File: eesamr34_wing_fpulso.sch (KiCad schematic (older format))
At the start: 19 parts, among them J3 Conn_01x02_Male, P1 SolderJumper_3_Bridged12, Q1 BS250, U2 4069

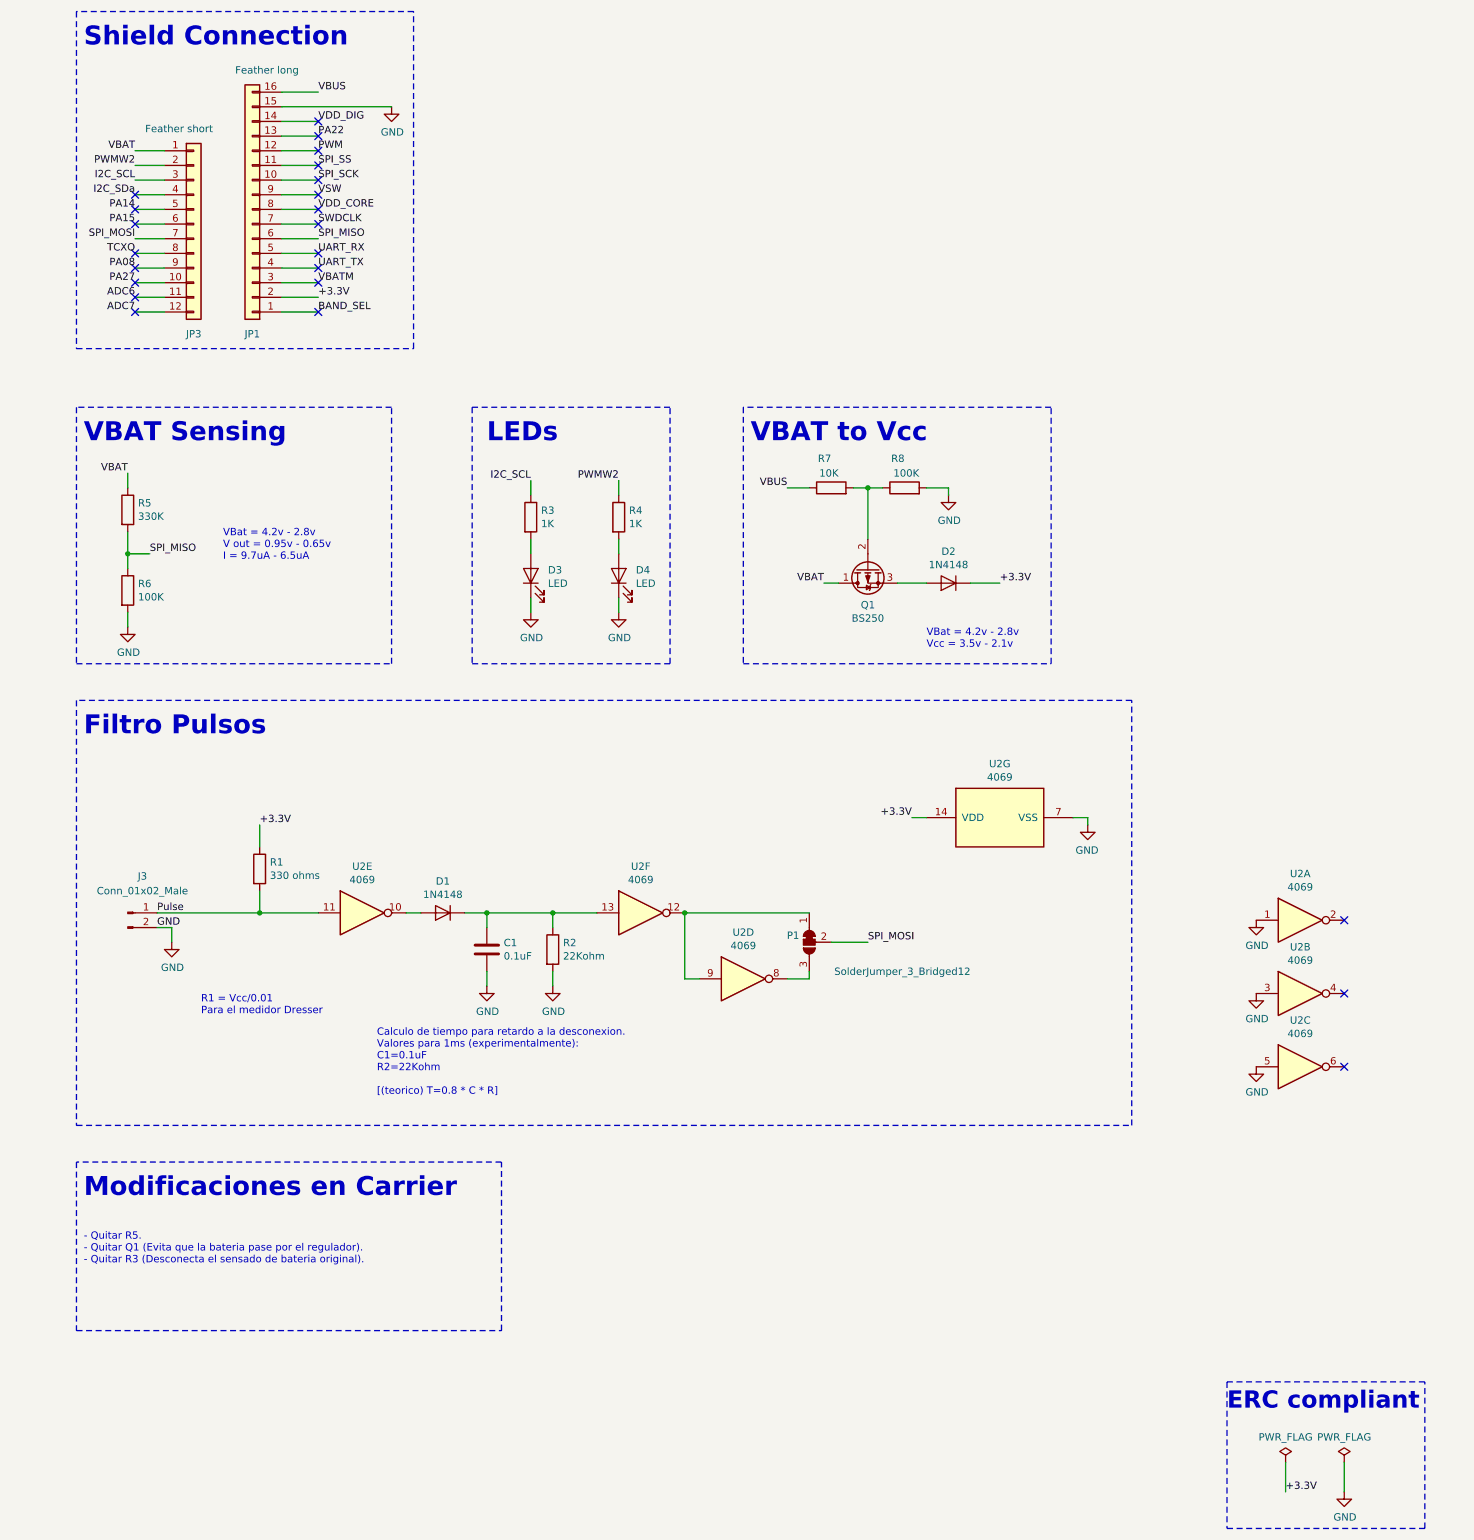
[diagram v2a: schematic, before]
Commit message: Reducido consumo de pullup y filtro
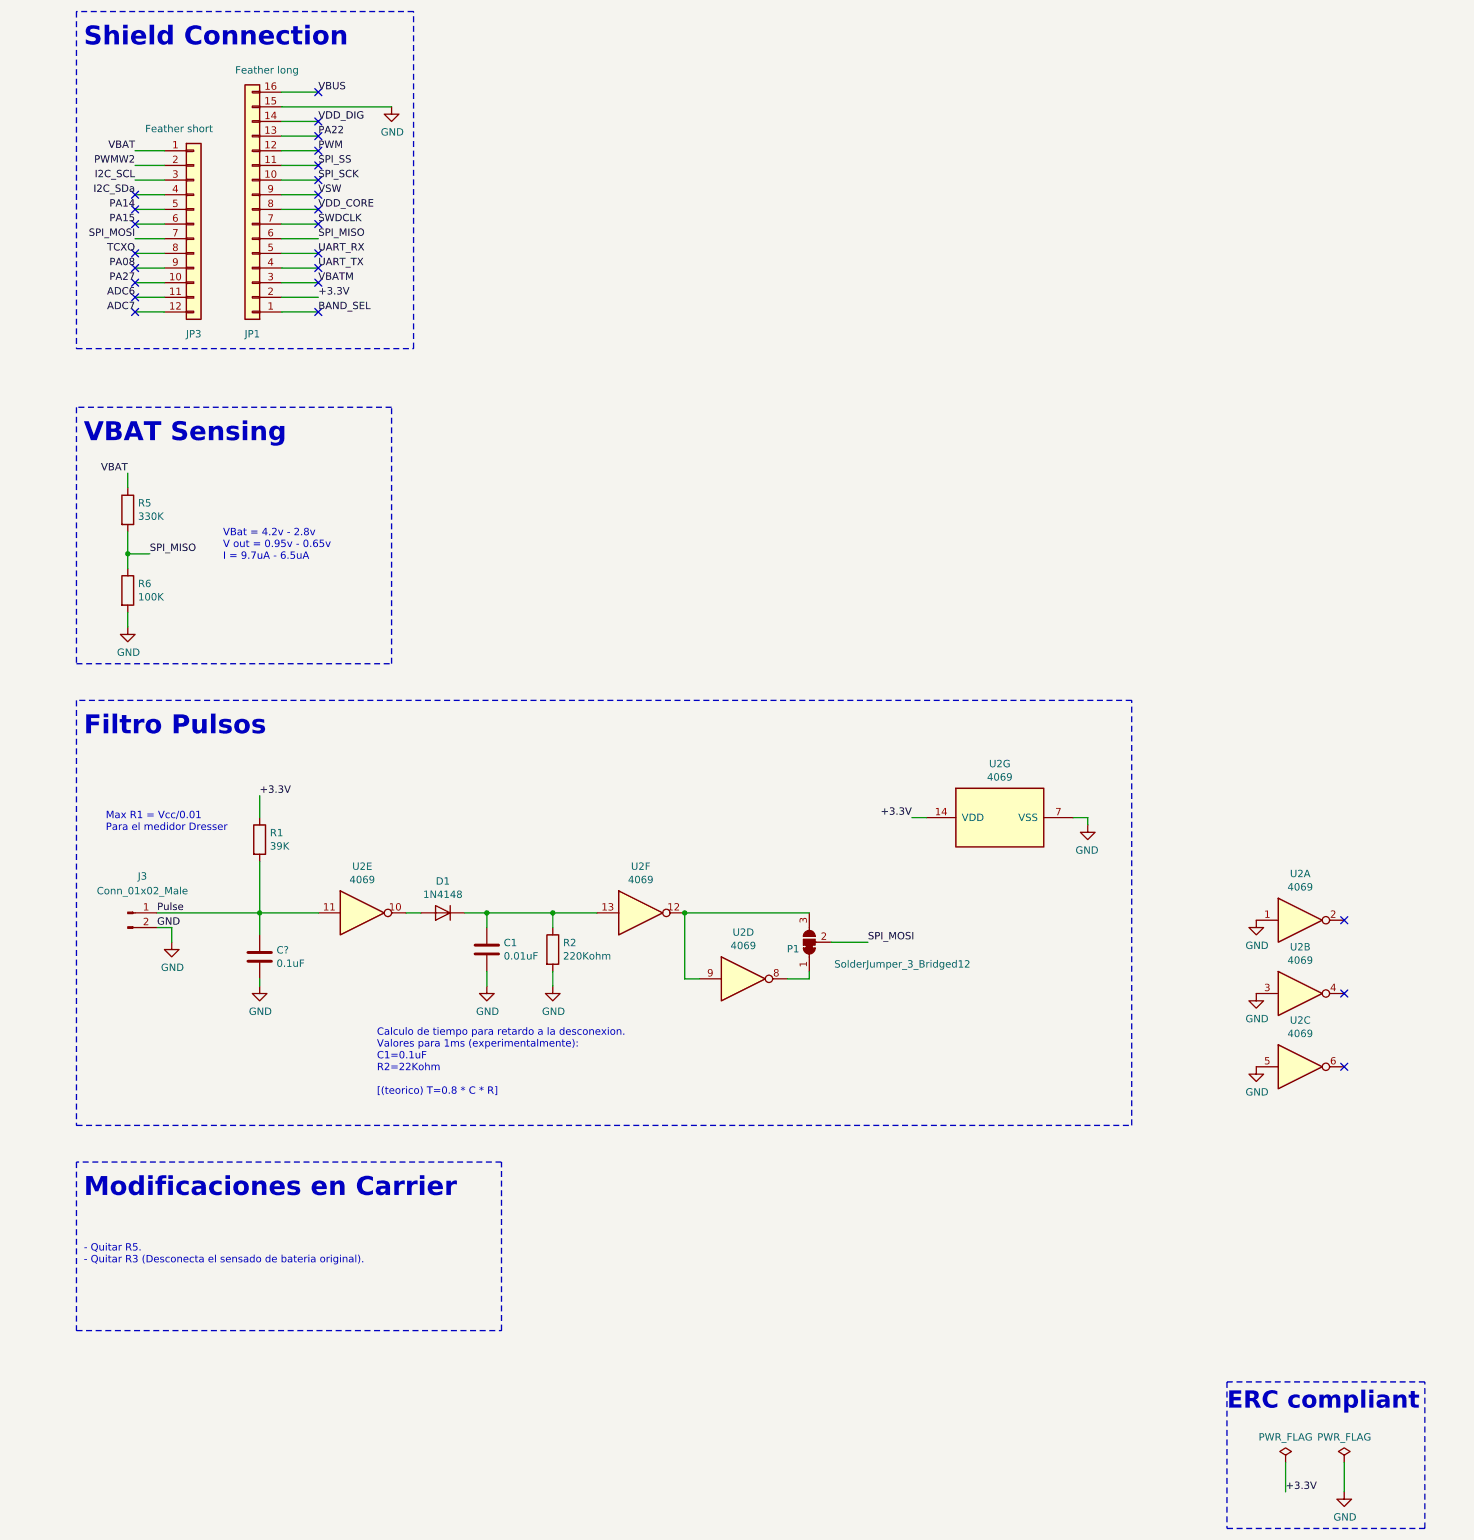
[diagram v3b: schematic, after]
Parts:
- removed D2: 1N4148, Diode_THT:D_DO-35_SOD27_P7.62mm_Horizontal, symbol Diode:1N4148
- removed D3, D4: LED, LED_THT:LED_D5.0mm, symbol Device:LED
- removed Q1: BS250, Package_TO_SOT_THT:TO-92_Inline, symbol Transistor_FET:BS250
- removed R3, R4: 1K, Resistor_THT:R_Axial_DIN0207_L6.3mm_D2.5mm_P10.16mm_Horizontal, symbol Device:R
- removed R7: 10K, Resistor_THT:R_Axial_DIN0207_L6.3mm_D2.5mm_P10.16mm_Horizontal, symbol Device:R
- removed R8: 100K, Resistor_THT:R_Axial_DIN0207_L6.3mm_D2.5mm_P10.16mm_Horizontal, symbol Device:R
- added C?: 0.1uF, Capacitor_THT:C_Disc_D5.0mm_W2.5mm_P2.50mm, symbol Device:C
- C1: value 0.1uF -> 0.01uF
- R1: value 330 ohms -> 39K
- R2: value 22Kohm -> 220Kohm
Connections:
- net GND: now also C?.2
- net Pulse: now also C?.1
- net at U2.12, U2.9: now also P1.3 (B); no longer P1.1 (A)
- net at U2.8: now also P1.1 (A); no longer P1.3 (B)
- no-connect marks 23 -> 24
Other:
- note added: "- Quitar R5.\n- Quitar R3 (Desconecta el sensado de bateria original)."
- note added: "Max R1 = Vcc/0.01\nPara el medidor Dresser"
- note removed: "- Quitar R5.\n- Quitar Q1 (Evita que la bateria pase por el regulador).\n- Quitar R3 (Desconecta el sensado de bateria original)."
- note removed: "LEDs"
- note removed: "R1 = Vcc/0.01\nPara el medidor Dresser"
- note removed: "VBAT to Vcc"
- note removed: "VBat = 4.2v - 2.8v\nVcc = 3.5v - 2.1v"
- moved on the sheet: R1
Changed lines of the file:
@@
 P 3800 7100
 F 0 "R2" H 3870 7146 50  0000 L CNN
-F 1 "22Kohm" H 3870 7055 50  0000 L CNN
+F 1 "220Kohm" H 3870 7055 50  0000 L CNN
 F 2 "Resistor_THT:R_Axial_DIN0207_L6.3mm_D2.5mm_P10.16mm_Horizontal" V 3730 7100 50  0001 C CNN
 F 3 "~" H 3800 7100 50  0001 C CNN
@@
 P 3350 7100
 F 0 "C1" H 3465 7146 50  0000 L CNN
-F 1 "0.1uF" H 3465 7055 50  0000 L CNN
+F 1 "0.01uF" H 3465 7055 50  0000 L CNN
 F 2 "Capacitor_THT:C_Disc_D5.0mm_W2.5mm_P2.50mm" H 3388 6950 50  0001 C CNN
 F 3 "~" H 3350 7100 50  0001 C CNN
@@
 L Device:R R1
 U 1 1 5F5899B8
-P 1800 6550
-F 0 "R1" H 1870 6596 50  0000 L CNN
-F 1 "330 ohms" H 1870 6505 50  0000 L CNN
-F 2 "Resistor_THT:R_Axial_DIN0207_L6.3mm_D2.5mm_P10.16mm_Horizontal" V 1730 6550 50  0001 C CNN
-F 3 "~" H 1800 6550 50  0001 C CNN
-	1    1800 6550
-	1    0    0    -1
-$EndComp
-Wire Wire Line
-	1800 6850 1800 6700
-Wire Wire Line
-	1800 6250 1800 6400
+P 1800 6350
+F 0 "R1" H 1870 6396 50  0000 L CNN
+F 1 "39K" H 1870 6305 50  0000 L CNN
+F 2 "Resistor_THT:R_Axial_DIN0207_L6.3mm_D2.5mm_P10.16mm_Horizontal" V 1730 6350 50  0001 C CNN
+F 3 "~" H 1800 6350 50  0001 C CNN
+	1    1800 6350
+	1    0    0    -1
+$EndComp
+Wire Wire Line
+	1800 6050 1800 6200
 Wire Wire Line
 	3350 6950 3350 6850
@@
 P 5550 7050
 F 0 "P1" V 5504 7118 50  0000 L CNN
-F 1 "SolderJumper_3_Bridged12" V 5750 5950 50  0000 L CNN
+F 1 "SolderJumper_3_Bridged12" V 5400 5950 50  0000 L CNN
 F 2 "Jumper:SolderJumper-3_P1.3mm_Bridged12_Pad1.0x1.5mm" H 5550 7050 50  0001 C CNN
 F 3 "~" H 5550 7050 50  0001 C CNN
 	1    5550 7050
-	0    -1   1    0
+	0    -1   -1   0
 $EndComp
 Wire Wire Line
@@
 Text Notes 2600 8100 0    50   ~ 0
 Calculo de tiempo para retardo a la desconexion.\nValores para 1ms (experimentalmente):\nC1=0.1uF\nR2=22Kohm\n\n[(teorico) T=0.8 * C * R]
-Text Notes 1400 7550 0    50   ~ 0
-R1 = Vcc/0.01\nPara el medidor Dresser
-Text Label 1800 6250 0    50   ~ 0
+Text Notes 750  6300 0    50   ~ 0
+Max R1 = Vcc/0.01\nPara el medidor Dresser
+Text Label 1800 6050 0    50   ~ 0
 +3.3V
 Text Notes 600  5650 0    129  ~ 26
@@
 ADC6
 Text Notes 600  9250 0    50   ~ 0
-- Quitar R5.\n- Quitar Q1 (Evita que la bateria pase por el regulador).\n- Quitar R3 (Desconecta el sensado de bateria original).
+- Quitar R5.\n- Quitar R3 (Desconecta el sensado de bateria original).
 Text Notes 600  8800 0    129  ~ 26
 Modificaciones en Carrier\n
@@
 Text Notes 1550 4450 0    50   ~ 0
 VBat = 4.2v - 2.8v\nV out = 0.95v - 0.65v\nI = 9.7uA - 6.5uA
-Text Notes 6350 5050 0    50   ~ 0
-VBat = 4.2v - 2.8v\nVcc = 3.5v - 2.1v
 Wire Wire Line
 	900  4400 900  4500
@@
 	1    0    0    -1
 $EndComp
-Text Notes 3350 3650 0    129  ~ 26
-LEDs
-Wire Wire Line
-	4250 3900 4250 4000
-Wire Wire Line
-	3650 3900 3650 4000
-Text Label 3650 3900 2    50   ~ 0
-I2C_SCL
-Text Label 4250 3900 2    50   ~ 0
-PWMW2
-Wire Wire Line
-	4250 4700 4250 4800
-Wire Wire Line
-	3650 4700 3650 4800
-Wire Wire Line
-	4250 4300 4250 4400
-Wire Wire Line
-	3650 4300 3650 4400
-$Comp
-L power:GND #PWR01
-U 1 1 5F964773
-P 4250 4800
-F 0 "#PWR01" H 4250 4550 50  0001 C CNN
-F 1 "GND" H 4255 4627 50  0000 C CNN
-F 2 "" H 4250 4800 50  0001 C CNN
-F 3 "" H 4250 4800 50  0001 C CNN
-	1    4250 4800
-	1    0    0    -1
-$EndComp
-$Comp
-L Device:LED D4
-U 1 1 5F96476D
-P 4250 4550
-F 0 "D4" V 4289 4433 50  0000 R CNN
-F 1 "LED" V 4198 4433 50  0000 R CNN
-F 2 "LED_THT:LED_D5.0mm" H 4250 4550 50  0001 C CNN
-F 3 "~" H 4250 4550 50  0001 C CNN
-	1    4250 4550
-	0    -1   -1   0
-$EndComp
-$Comp
-L Device:R R4
-U 1 1 5F964767
-P 4250 4150
-F 0 "R4" H 4320 4196 50  0000 L CNN
-F 1 "1K" H 4320 4105 50  0000 L CNN
-F 2 "Resistor_THT:R_Axial_DIN0207_L6.3mm_D2.5mm_P10.16mm_Horizontal" V 4180 4150 50  0001 C CNN
-F 3 "~" H 4250 4150 50  0001 C CNN
-	1    4250 4150
-	1    0    0    -1
-$EndComp
-Text Notes 5150 3650 0    129  ~ 26
-VBAT to Vcc
-Wire Wire Line
-	6650 4600 6850 4600
-Wire Wire Line
-	6150 4600 6350 4600
-Text Label 6850 4600 0    50   ~ 0
-+3.3V
-Text Label 5650 4600 2    50   ~ 0
-VBAT
-$Comp
-L Diode:1N4148 D2
-U 1 1 5F937EA6
-P 6500 4600
-F 0 "D2" H 6500 4384 50  0000 C CNN
-F 1 "1N4148" H 6500 4475 50  0000 C CNN
-F 2 "Diode_THT:D_DO-35_SOD27_P7.62mm_Horizontal" H 6500 4425 50  0001 C CNN
-F 3 "https://assets.nexperia.com/documents/data-sheet/1N4148_1N4448.pdf" H 6500 4600 50  0001 C CNN
-	1    6500 4600
-	-1   0    0    1
-$EndComp
-$Comp
-L power:GND #PWR0106
-U 1 1 5F5899F4
-P 3650 4800
-F 0 "#PWR0106" H 3650 4550 50  0001 C CNN
-F 1 "GND" H 3655 4627 50  0000 C CNN
-F 2 "" H 3650 4800 50  0001 C CNN
-F 3 "" H 3650 4800 50  0001 C CNN
-	1    3650 4800
-	1    0    0    -1
-$EndComp
-$Comp
-L Device:LED D3
-U 1 1 5F5899EE
-P 3650 4550
-F 0 "D3" V 3689 4433 50  0000 R CNN
-F 1 "LED" V 3598 4433 50  0000 R CNN
-F 2 "LED_THT:LED_D5.0mm" H 3650 4550 50  0001 C CNN
-F 3 "~" H 3650 4550 50  0001 C CNN
-	1    3650 4550
-	0    -1   -1   0
-$EndComp
-$Comp
-L Device:R R3
-U 1 1 5F5899E8
-P 3650 4150
-F 0 "R3" H 3720 4196 50  0000 L CNN
-F 1 "1K" H 3720 4105 50  0000 L CNN
-F 2 "Resistor_THT:R_Axial_DIN0207_L6.3mm_D2.5mm_P10.16mm_Horizontal" V 3580 4150 50  0001 C CNN
-F 3 "~" H 3650 4150 50  0001 C CNN
-	1    3650 4150
-	1    0    0    -1
-$EndComp
-$Comp
-L Transistor_FET:BS250 Q1
-U 1 1 5FAA13A5
-P 5950 4500
-F 0 "Q1" V 6199 4500 50  0000 C CNN
-F 1 "BS250" V 6290 4500 50  0000 C CNN
-F 2 "Package_TO_SOT_THT:TO-92_Inline" H 6150 4425 50  0001 L CIN
-F 3 "http://www.vishay.com/docs/70209/70209.pdf" H 5950 4500 50  0001 L CNN
-	1    5950 4500
-	0    -1   1    0
-$EndComp
-Wire Wire Line
-	5650 4600 5750 4600
-$Comp
-L Device:R R8
-U 1 1 5FAA87B2
-P 6200 3950
-F 0 "R8" V 6400 3950 50  0000 L CNN
-F 1 "100K" V 6300 3850 50  0000 L CNN
-F 2 "Resistor_THT:R_Axial_DIN0207_L6.3mm_D2.5mm_P10.16mm_Horizontal" V 6130 3950 50  0001 C CNN
-F 3 "~" H 6200 3950 50  0001 C CNN
-	1    6200 3950
-	0    -1   -1   0
-$EndComp
-$Comp
-L power:GND #PWR05
-U 1 1 5FAA8E51
-P 6500 4000
-F 0 "#PWR05" H 6500 3750 50  0001 C CNN
-F 1 "GND" H 6505 3827 50  0000 C CNN
-F 2 "" H 6500 4000 50  0001 C CNN
-F 3 "" H 6500 4000 50  0001 C CNN
-	1    6500 4000
-	1    0    0    -1
-$EndComp
-Text Label 5400 3950 2    50   ~ 0
-VBUS
-Wire Wire Line
-	5400 3950 5550 3950
-Wire Wire Line
-	5950 4300 5950 3950
-Wire Wire Line
-	5950 3950 5850 3950
-$Comp
-L Device:R R7
-U 1 1 5FAA7900
-P 5700 3950
-F 0 "R7" V 5900 3950 50  0000 L CNN
-F 1 "10K" V 5800 3900 50  0000 L CNN
-F 2 "Resistor_THT:R_Axial_DIN0207_L6.3mm_D2.5mm_P10.16mm_Horizontal" V 5630 3950 50  0001 C CNN
-F 3 "~" H 5700 3950 50  0001 C CNN
-	1    5700 3950
-	0    -1   -1   0
-$EndComp
-Wire Notes Line
-	5100 3400 5100 5150
-Wire Notes Line
-	5100 5150 7200 5150
-Wire Notes Line
-	7200 5150 7200 3400
-Wire Notes Line
-	7200 3400 5100 3400
-Wire Wire Line
-	6500 3950 6500 4000
-Wire Wire Line
-	5950 3950 6050 3950
-Connection ~ 5950 3950
-Wire Wire Line
-	6350 3950 6500 3950
-Wire Notes Line
-	3250 3400 3250 5150
-Wire Notes Line
-	3250 5150 4600 5150
-Wire Notes Line
-	4600 5150 4600 3400
-Wire Notes Line
-	4600 3400 3250 3400
 NoConn ~ 950  2650
 $Comp
@@
 $EndComp
 $Comp
-L power:GND #PWR?
+L power:GND #PWR0105
 U 1 1 5F98C2FD
 P 8600 6900
-F 0 "#PWR?" H 8600 6650 50  0001 C CNN
+F 0 "#PWR0105" H 8600 6650 50  0001 C CNN
 F 1 "GND" H 8605 6727 50  0000 C CNN
 F 2 "" H 8600 6900 50  0001 C CNN
@@
 $EndComp
 $Comp
-L power:GND #PWR?
+L power:GND #PWR0107
 U 1 1 5F98D849
 P 8600 7400
-F 0 "#PWR?" H 8600 7150 50  0001 C CNN
+F 0 "#PWR0107" H 8600 7150 50  0001 C CNN
 F 1 "GND" H 8605 7227 50  0000 C CNN
 F 2 "" H 8600 7400 50  0001 C CNN
@@
 $EndComp
 $Comp
-L power:GND #PWR?
+L power:GND #PWR0108
 U 1 1 5F98E314
 P 8600 7900
-F 0 "#PWR?" H 8600 7650 50  0001 C CNN
+F 0 "#PWR0108" H 8600 7650 50  0001 C CNN
 F 1 "GND" H 8605 7727 50  0000 C CNN
 F 2 "" H 8600 7900 50  0001 C CNN
@@
 Text Label 5950 7050 0    50   ~ 0
 SPI_MOSI
+NoConn ~ 2200 1250
+$Comp
+L Device:C C?
+U 1 1 5FA241A0
+P 1800 7150
+F 0 "C?" H 1915 7196 50  0000 L CNN
+F 1 "0.1uF" H 1915 7105 50  0000 L CNN
+F 2 "Capacitor_THT:C_Disc_D5.0mm_W2.5mm_P2.50mm" H 1838 7000 50  0001 C CNN
+F 3 "~" H 1800 7150 50  0001 C CNN
+	1    1800 7150
+	1    0    0    -1
+$EndComp
+$Comp
+L power:GND #PWR?
+U 1 1 5FA26127
+P 1800 7350
+F 0 "#PWR?" H 1800 7100 50  0001 C CNN
+F 1 "GND" H 1805 7177 50  0000 C CNN
+F 2 "" H 1800 7350 50  0001 C CNN
+F 3 "" H 1800 7350 50  0001 C CNN
+	1    1800 7350
+	1    0    0    -1
+$EndComp
+Wire Wire Line
+	1800 6500 1800 6850
+Wire Wire Line
+	1800 6850 1800 7000
+Wire Wire Line
+	1800 7300 1800 7350
 $EndSCHEMATC
